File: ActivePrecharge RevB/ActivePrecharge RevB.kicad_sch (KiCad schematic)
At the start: 26 parts, among them J1 Conn_01x03, J2 Conn_01x04, U1 PAMC0311SQDWVRQ1, U2 PAMC0311SQDWVRQ1

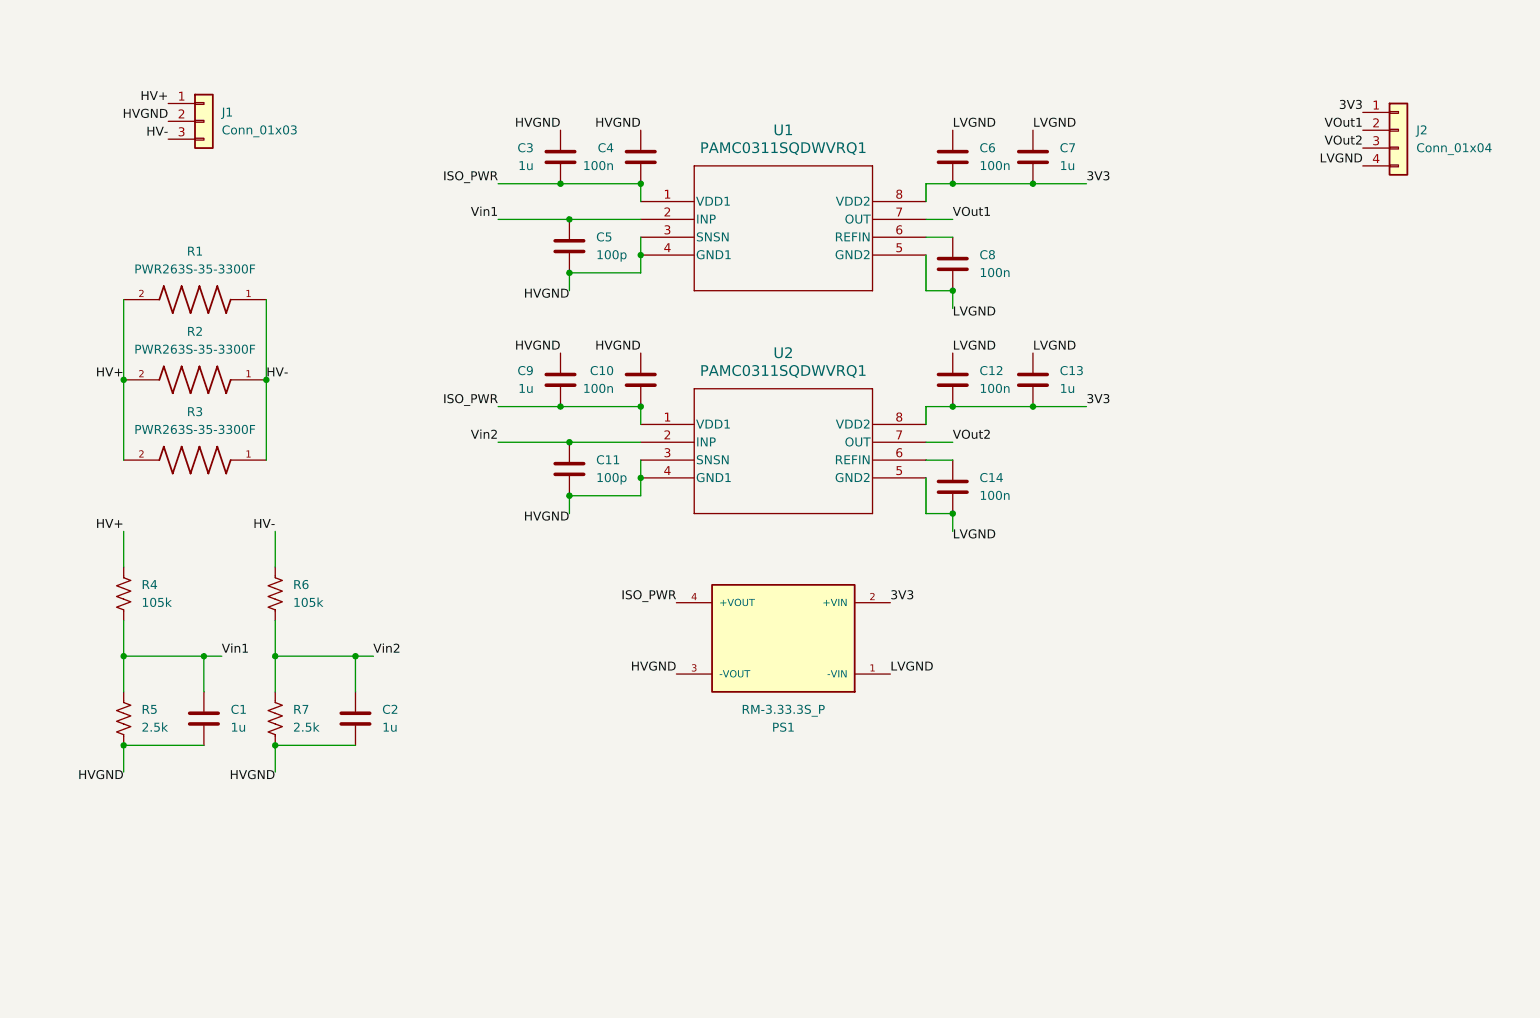
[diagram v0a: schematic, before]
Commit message: Active Precharge Rev A with LDO and 3.3-5 ISO
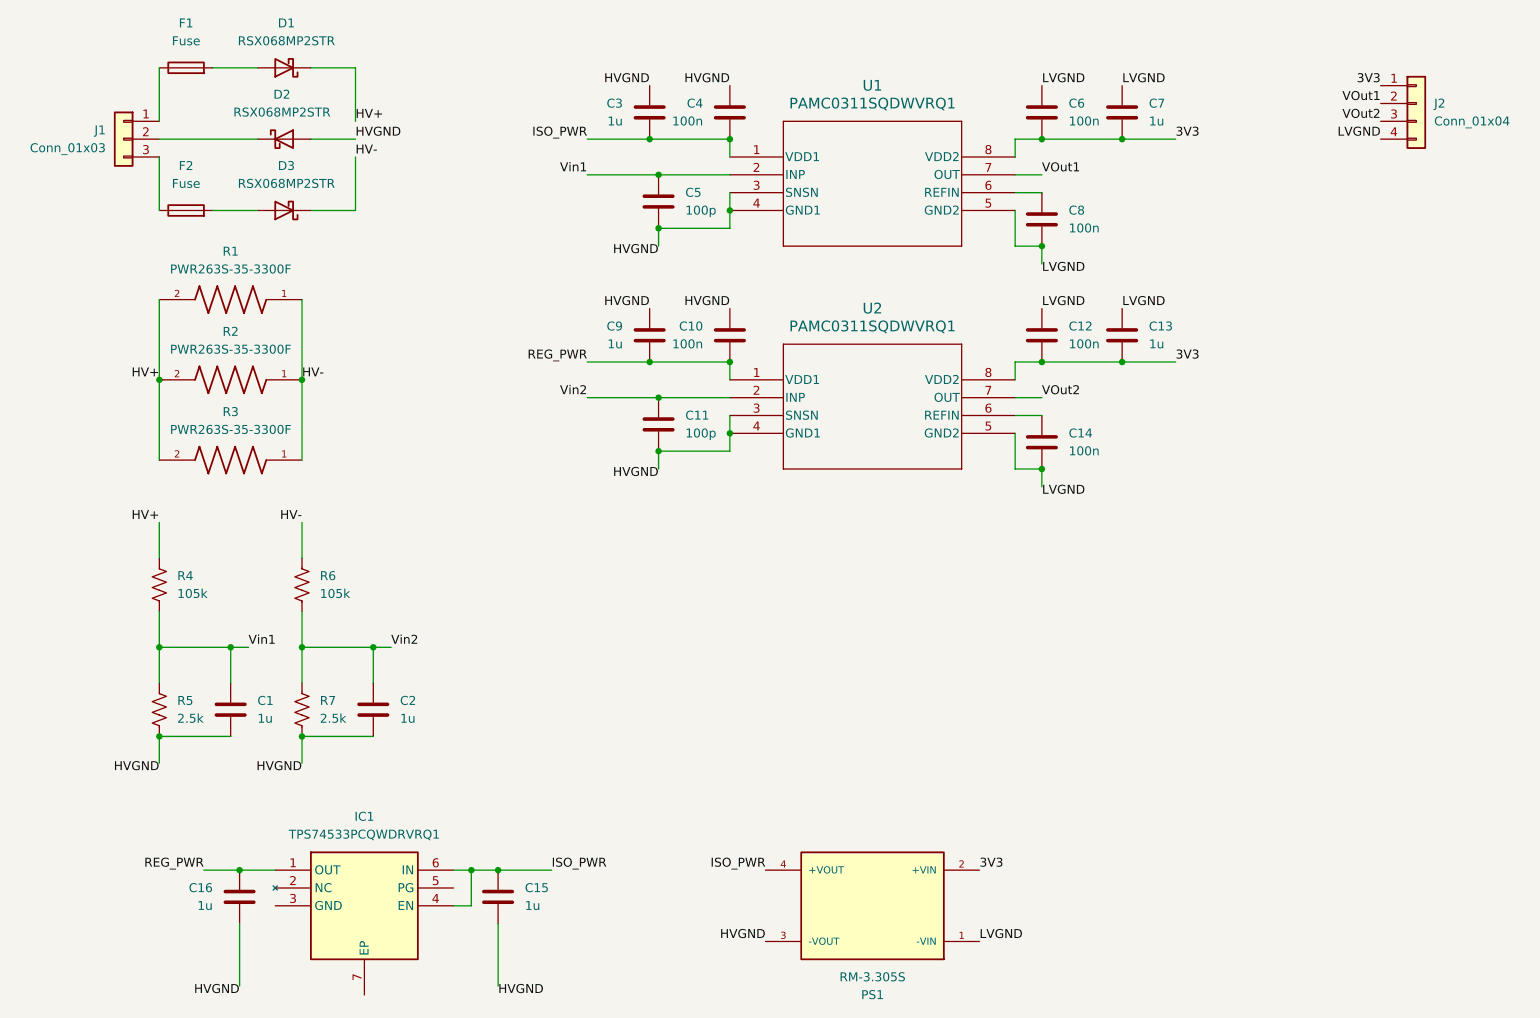
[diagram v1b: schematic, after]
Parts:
- removed PS1: RM-3.33.3S_P, RM-3.33.3S_P:CONV_RM-3.33.3S_P, symbol ISO-DCDC:RM-3.33.3S_P
- added C15, C16: 1u, symbol Device:C
- added D1, D2, D3: RSX068MP2STR, ActivePrecharge-RevB:RSX068MP2STR, symbol Device:D_Schottky
- added F1, F2: Fuse, symbol Device:Fuse
- added IC1: TPS74533PCQWDRVRQ1, SON65P200X200X80-7N, symbol LDO:TPS74533PCQWDRVRQ1
- added PS1: RM-3.305S, RM-3.305S:CONV_RM-3.305S, symbol ISO-DCDC5:RM-3.305S
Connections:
- net 3V3: now also PS1.2 (+VIN)
- net HV+: now also D1.1 (K); no longer J1.1 (Pin_1)
- net HV-: now also D3.1 (K); no longer J1.3 (Pin_3)
- net HVGND: now also C15.2, C16.2, D2.2 (A), PS1.3 (-VOUT); no longer J1.2 (Pin_2)
- net ISO_PWR: now also C15.1, IC1.4 (EN), IC1.6 (IN), PS1.4 (+VOUT); no longer C10.2, C9.2, U2.1 (VDD1)
- net LVGND: now also PS1.1 (-VIN)
- new net: F1.1, J1.1 (Pin_1)
- new net: D2.1 (K), J1.2 (Pin_2)
- new net: F2.1, J1.3 (Pin_3)
- new net: D3.2 (A), F2.2
- new net: D1.2 (A), F1.2
- new net REG_PWR: C10.2, C16.1, C9.2, IC1.1 (OUT), U2.1 (VDD1)
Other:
- moved on the sheet: C1, C10, C11, C12, C13, C14, C2, C3, C4, C5, C6, C7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
